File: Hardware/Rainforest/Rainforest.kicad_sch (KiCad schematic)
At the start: 36 parts, among them J1 Conn_01x08_Pin, U1 STM32F401CCUx, U2 LY68L6400, Y1 32768 Hz, Y2 25MHz

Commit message: - Still working on font
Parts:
- added C18: 4.7uF, symbol Device:C
- added C19: 100nF, symbol Device:C
- added J2: Conn_01x06_Pin, symbol Connector:Conn_01x06_Pin
- added R14: 10k, symbol Device:R
- added R7: 100, symbol Device:R
- renumbered C18 to C17, R8 to R10, R9 to R11, R10 to R12, R11 to R13, R4 to R2, R12 to R3, R2 to R4, R3 to R5, R5 to R6, R6 to R8, R7 to R9
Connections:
- net GND: now also C18.2, C19.2, J2.6 (Pin_6)
- net REG_3.3: now also C18.1, C19.1, J2.1 (Pin_1), R14.1
- net SPI1_MISO: now also J2.5 (Pin_5), R14.2
- net SPI1_MOSI: now also J2.3 (Pin_3)
- net SPI1_SCK: now also J2.4 (Pin_4)
- net at U1.41 (PB5): now also R7.2
- new net SD_#CS: J2.2 (Pin_2), R7.1
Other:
- note added: "3.3V"
- note added: "CLK"
- note added: "MISO"
- note added: "Micro SD"
- note added: "MicroSD Adapter"
- note added: "SD Card pull-up"

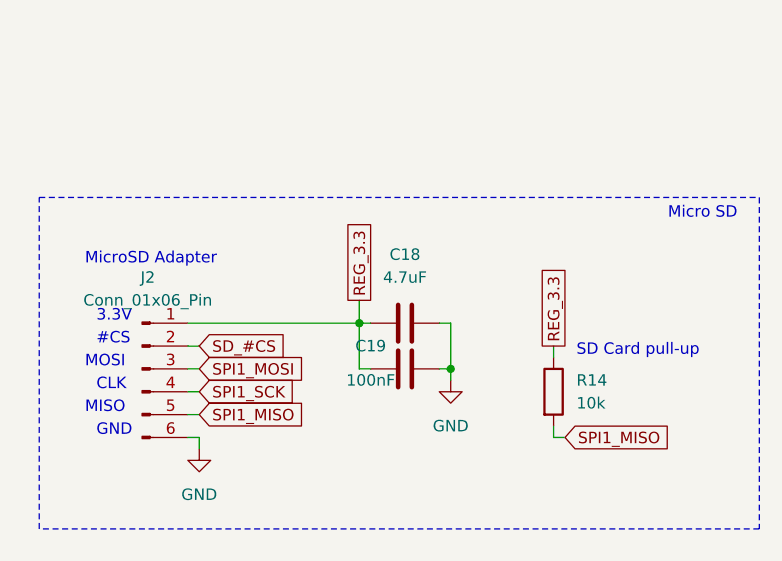
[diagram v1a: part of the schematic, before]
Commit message: Fixed pSRAM "failure" due to non-initialized SD-card
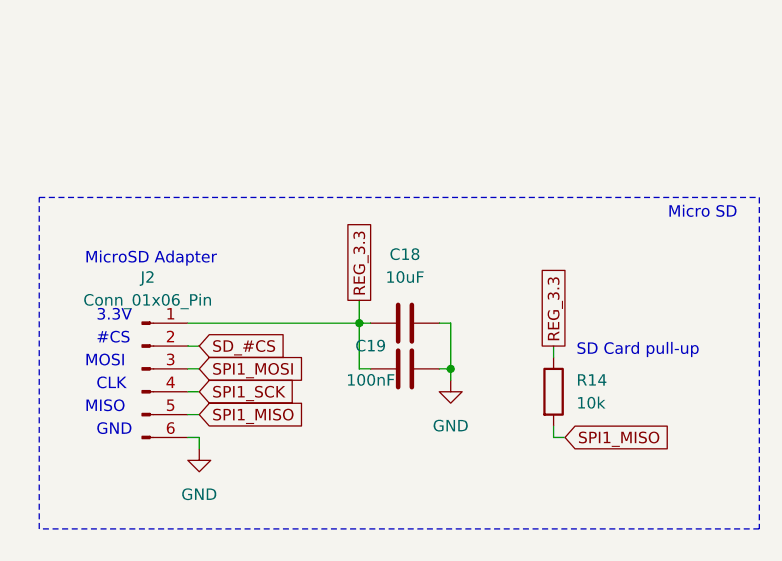
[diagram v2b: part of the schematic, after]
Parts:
- C18: value 4.7uF -> 10uF
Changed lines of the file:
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@@
 			)
 		)
-		(property "Value" "4.7uF"
+		(property "Value" "10uF"
 			(at 408.94 114.3 90)
 			(effects
